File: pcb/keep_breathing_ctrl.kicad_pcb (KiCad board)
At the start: 4 copper layers, 112 x 131 mm, 177 parts, among them J2 Screw_Terminal, P1 CONN_RASPBERRY, Q1 PN2222, Q2 PN2222, U1 MPL3115A2, U10 PCF8523TK, U11 AQH3213AX, U12 AQH3213AX, U13 HTS221, U14 ICE40UP5K-SG48ITR, U15 GD25Q32CTIGR-Memory_Flash, U16 UCC12040, U17 ISO7762, U18 ZLDO1117G33TA, U2 powerSTEP01, U3 TLP240D, U4 TLP240D, U5 TLP240D, U6 TLP240D, U7 TLP240D, U8 TLP240D, U9 ZLDO1117G33TA, Y1 ABS06-107-32.768KHZ-T

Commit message: connecting SPI signals from STM32
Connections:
- U14 pad 10: (no net) -> /STM32F4/SPI3_MISO
- U14 pad 11: (no net) -> /STM32F4/SPI3_MOSI
- U14 pad 9: (no net) -> /STM32F4/SPI3_SCK
- U17 pad 5: (no net) -> /Power Stepper/M_CS
- UST1 pad 1: (no net) -> /Power Stepper/M_CLK
- UST1 pad 3: (no net) -> /Power Stepper/M_CS
- UST1 pad 4: (no net) -> /Power Stepper/M_MISO
- UST1 pad 5: (no net) -> /Power Stepper/M_MOSI
- UST1 pad 78: /Power Stepper/M_CLK -> /STM32F4/SPI3_SCK
- UST1 pad 79: /Power Stepper/M_MISO -> /STM32F4/SPI3_MISO
- UST1 pad 80: /Power Stepper/M_MOSI -> /STM32F4/SPI3_MOSI
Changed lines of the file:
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@@
     (zones 0)
     (modules 177)
-    (nets 137)
+    (nets 141)
   )
   (page A4)
@@
   (net 135 /SensorShields/SPI_CS_4)
   (net 136 /SensorShields/I2C_CLK_4)
+  (net 137 /STM32F4/SPI3_MOSI)
+  (net 138 /STM32F4/SPI3_MISO)
+  (net 139 /STM32F4/SPI3_SCK)
+  (net 140 "/Power Stepper/M_CS")
   (net_class Default "This is the default net class."
     (clearance 0.2)
@@
     (add_net /STM32F4/SDIO_D0)
     (add_net /STM32F4/SDIO_D1)
+    (add_net /STM32F4/SPI3_MISO)
+    (add_net /STM32F4/SPI3_MOSI)
+    (add_net /STM32F4/SPI3_SCK)
     (add_net /STM32F4/STM_I2C1_SCL)
     (add_net /STM32F4/STM_I2C1_SDA)
@@
     (add_net /SensorShields/SPI_MISO)
     (add_net /SensorShields/SPI_MOSI)
-    (add_net /SensorShields/SS_SPI_CLK)
     (add_net /SensorShields/SS_SPI_CS)
-    (add_net /SensorShields/SS_SPI_MISO)
-    (add_net /SensorShields/SS_SPI_MOSI)
     (add_net /SensorShields/VCC_PLL)
     (add_net /Sensors/SCL)
@@
     (add_net "Net-(U2-Pad63)")
     (add_net "Net-(U2-Pad64)")
-    (add_net "Net-(UST1-Pad1)")
     (add_net "Net-(UST1-Pad15)")
     (add_net "Net-(UST1-Pad16)")
     (add_net "Net-(UST1-Pad18)")
     (add_net "Net-(UST1-Pad2)")
-    (add_net "Net-(UST1-Pad3)")
     (add_net "Net-(UST1-Pad36)")
     (add_net "Net-(UST1-Pad38)")
-    (add_net "Net-(UST1-Pad4)")
     (add_net "Net-(UST1-Pad47)")
-    (add_net "Net-(UST1-Pad5)")
     (add_net "Net-(UST1-Pad55)")
     (add_net "Net-(UST1-Pad56)")
@@
     (pad 12 smd roundrect (at -3.4375 -2.75 315) (size 0.875 0.25) (layers B.Cu B.Paste B.Mask) (roundrect_rratio 0.25)
       (net 88 /SensorShields/I2C_CLK_2))
-    (pad 11 smd roundrect (at -3.4375 -2.25 315) (size 0.875 0.25) (layers B.Cu B.Paste B.Mask) (roundrect_rratio 0.25))
-    (pad 10 smd roundrect (at -3.4375 -1.75 315) (size 0.875 0.25) (layers B.Cu B.Paste B.Mask) (roundrect_rratio 0.25))
-    (pad 9 smd roundrect (at -3.4375 -1.25 315) (size 0.875 0.25) (layers B.Cu B.Paste B.Mask) (roundrect_rratio 0.25))
+    (pad 11 smd roundrect (at -3.4375 -2.25 315) (size 0.875 0.25) (layers B.Cu B.Paste B.Mask) (roundrect_rratio 0.25)
+      (net 137 /STM32F4/SPI3_MOSI))
+    (pad 10 smd roundrect (at -3.4375 -1.75 315) (size 0.875 0.25) (layers B.Cu B.Paste B.Mask) (roundrect_rratio 0.25)
+      (net 138 /STM32F4/SPI3_MISO))
+    (pad 9 smd roundrect (at -3.4375 -1.25 315) (size 0.875 0.25) (layers B.Cu B.Paste B.Mask) (roundrect_rratio 0.25)
+      (net 139 /STM32F4/SPI3_SCK))
     (pad 8 smd roundrect (at -3.4375 -0.75 315) (size 0.875 0.25) (layers B.Cu B.Paste B.Mask) (roundrect_rratio 0.25)
       (net 79 /SensorShields/CRESET_N))
@@
     (pad 81 smd roundrect (at 3.5 7.675 315) (size 0.3 1.6) (layers B.Cu B.Paste B.Mask) (roundrect_rratio 0.25))
     (pad 80 smd roundrect (at 4 7.675 315) (size 0.3 1.6) (layers B.Cu B.Paste B.Mask) (roundrect_rratio 0.25)
-      (net 57 "/Power Stepper/M_MOSI"))
+      (net 137 /STM32F4/SPI3_MOSI))
     (pad 79 smd roundrect (at 4.5 7.675 315) (size 0.3 1.6) (layers B.Cu B.Paste B.Mask) (roundrect_rratio 0.25)
-      (net 56 "/Power Stepper/M_MISO"))
+      (net 138 /STM32F4/SPI3_MISO))
     (pad 78 smd roundrect (at 5 7.675 315) (size 0.3 1.6) (layers B.Cu B.Paste B.Mask) (roundrect_rratio 0.25)
-      (net 58 "/Power Stepper/M_CLK"))
+      (net 139 /STM32F4/SPI3_SCK))
     (pad 77 smd roundrect (at 5.5 7.675 315) (size 0.3 1.6) (layers B.Cu B.Paste B.Mask) (roundrect_rratio 0.25)
       (net 130 /Rapsberry/JTDI))
@@
     (pad 6 smd roundrect (at -7.675 3.5 315) (size 1.6 0.3) (layers B.Cu B.Paste B.Mask) (roundrect_rratio 0.25)
       (net 59 +3.3VP))
-    (pad 5 smd roundrect (at -7.675 4 315) (size 1.6 0.3) (layers B.Cu B.Paste B.Mask) (roundrect_rratio 0.25))
-    (pad 4 smd roundrect (at -7.675 4.5 315) (size 1.6 0.3) (layers B.Cu B.Paste B.Mask) (roundrect_rratio 0.25))
-    (pad 3 smd roundrect (at -7.675 5 315) (size 1.6 0.3) (layers B.Cu B.Paste B.Mask) (roundrect_rratio 0.25))
+    (pad 5 smd roundrect (at -7.675 4 315) (size 1.6 0.3) (layers B.Cu B.Paste B.Mask) (roundrect_rratio 0.25)
+      (net 57 "/Power Stepper/M_MOSI"))
+    (pad 4 smd roundrect (at -7.675 4.5 315) (size 1.6 0.3) (layers B.Cu B.Paste B.Mask) (roundrect_rratio 0.25)
+      (net 56 "/Power Stepper/M_MISO"))
+    (pad 3 smd roundrect (at -7.675 5 315) (size 1.6 0.3) (layers B.Cu B.Paste B.Mask) (roundrect_rratio 0.25)
+      (net 140 "/Power Stepper/M_CS"))
     (pad 2 smd roundrect (at -7.675 5.5 315) (size 1.6 0.3) (layers B.Cu B.Paste B.Mask) (roundrect_rratio 0.25))
-    (pad 1 smd roundrect (at -7.675 6 315) (size 1.6 0.3) (layers B.Cu B.Paste B.Mask) (roundrect_rratio 0.25))
+    (pad 1 smd roundrect (at -7.675 6 315) (size 1.6 0.3) (layers B.Cu B.Paste B.Mask) (roundrect_rratio 0.25)
+      (net 58 "/Power Stepper/M_CLK"))
     (model ${KISYS3DMOD}/Package_QFP.3dshapes/LQFP-100_14x14mm_P0.5mm.wrl
       (at (xyz 0 0 0))
@@
     (pad 6 smd rect (at -2.6 -0.9525 90) (size 1.2 0.4) (layers B.Cu B.Paste B.Mask)
       (net 56 "/Power Stepper/M_MISO"))
-    (pad 5 smd rect (at -2.6 -0.3175 90) (size 1.2 0.4) (layers B.Cu B.Paste B.Mask))
+    (pad 5 smd rect (at -2.6 -0.3175 90) (size 1.2 0.4) (layers B.Cu B.Paste B.Mask)
+      (net 140 "/Power Stepper/M_CS"))
     (pad 4 smd rect (at -2.6 0.3175 90) (size 1.2 0.4) (layers B.Cu B.Paste B.Mask)
       (net 58 "/Power Stepper/M_CLK"))

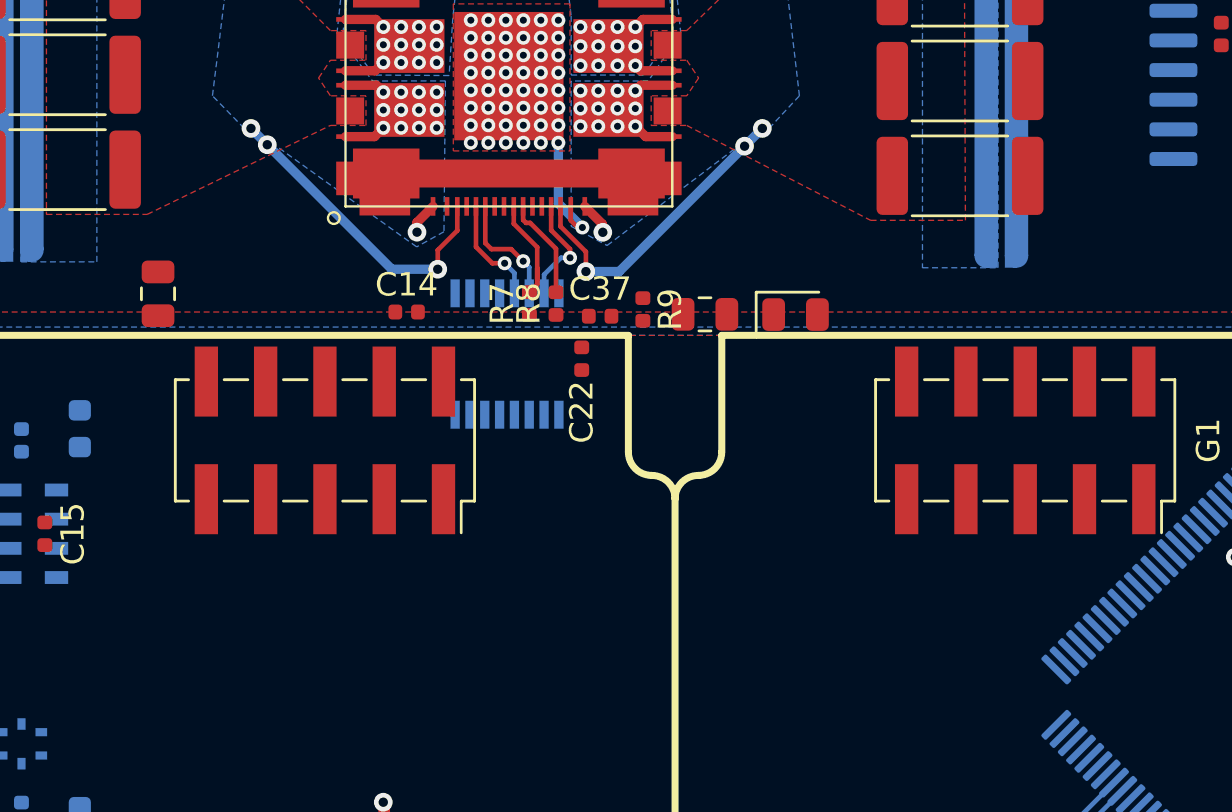
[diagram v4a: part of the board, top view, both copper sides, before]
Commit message: routing spi from stepper driver
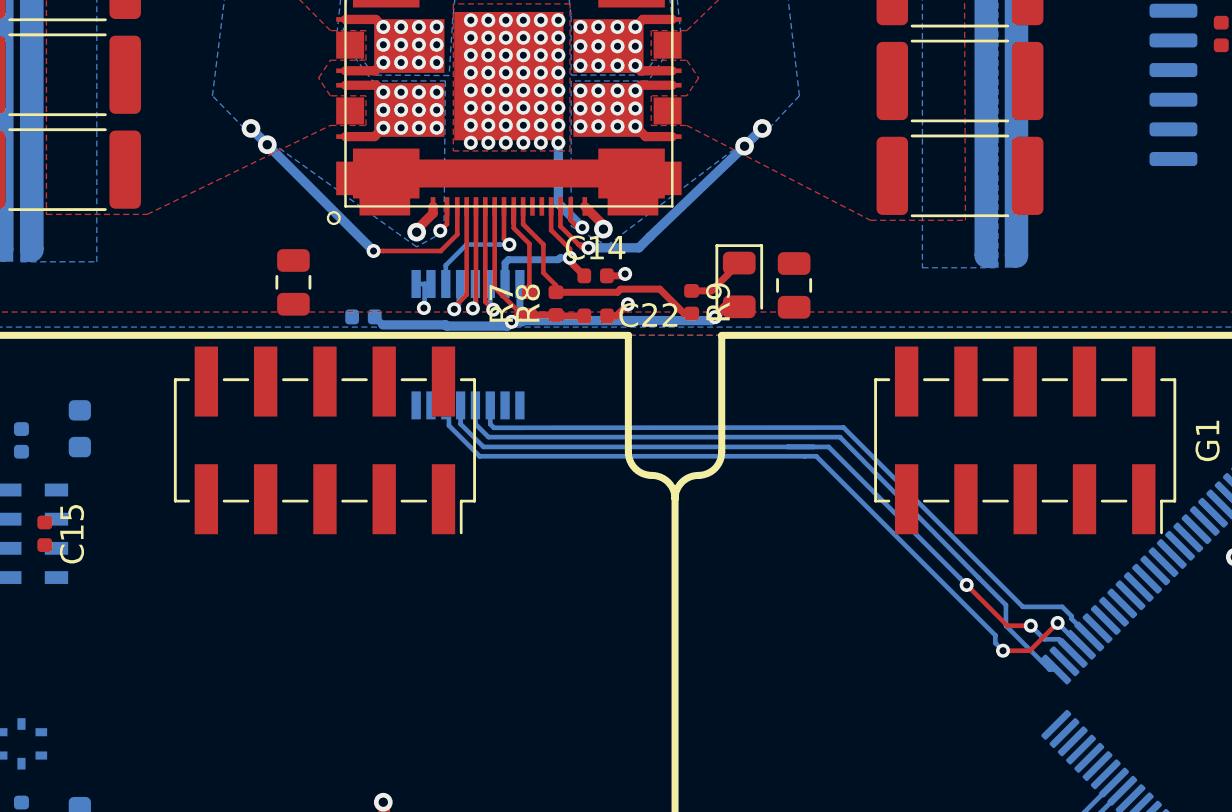
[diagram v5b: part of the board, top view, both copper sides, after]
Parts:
- C37: moved to B.Cu
- moved C37 10.1 mm to (97.2, 66.2), turned to 180 degrees
- moved C14 8.24 mm to (107.1, 64.5)
- moved C6 5.82 mm to (94.2, 64.7)
- moved C7 4.02 mm to (115.6, 64.9), turned to 270 degrees
- moved D5 2.72 mm to (113.2, 64.8), turned to 270 degrees
- moved R9 2.11 mm to (111.2, 65.6)
- moved C22 1.93 mm to (107.1, 66.2), turned to 0 degrees
- moved U17 1.72 mm to (101.6, 67.4)
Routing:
- net /Power Stepper/M_MISO: track 0.00 -> 33.1 mm, vias 0 -> 2
- net /Power Stepper/M_CS: track 0.00 -> 32.2 mm, vias 0 -> 2
- net /Power Stepper/M_CLK: track 0.00 -> 30.6 mm
- net /Power Stepper/M_MOSI: track 0.00 -> 30.3 mm
- net 3V3_M: track 18.4 -> 45.5 mm, vias 1 -> 3
- net SM_FLAG: track 4.36 -> 10.6 mm
- net /Power Stepper/SM_CS: track 0.00 -> 5.82 mm, vias 0 -> 1
- net /Power Stepper/SM_SO: track 0.00 -> 5.62 mm, vias 0 -> 1
- net GND_MOTOR: track 14.8 -> 19.6 mm, vias 54 -> 58
- net /Power Stepper/SM_RST: track 4.75 -> 7.34 mm
- net Net-(D5-Pad1): track 0.00 -> 2.53 mm
- net Net-(JP2-Pad1): track 13.5 -> 12.5 mm
- net Net-(JP1-Pad1): track 13.3 -> 12.4 mm
- net /Power Stepper/SM_CLK: track 4.72 -> 5.52 mm
- net /Power Stepper/SM_SI: track 5.00 -> 5.72 mm

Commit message: protection circuit added
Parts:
- removed C16, C76: 33u, Capacitor_SMD:C_1206_3216Metric
- removed C17: 220u, Capacitor_SMD:C_1206_3216Metric
- removed C18: 0.1u, Capacitor_SMD:C_0603_1608Metric
- removed C19: 1n, Capacitor_SMD:C_0603_1608Metric
- removed C77: 2.2uF, Capacitor_SMD:C_0603_1608Metric
- removed C79: 0.1u, Capacitor_SMD:C_0402_1005Metric
- removed D6: LED, LED_SMD:LED_0805_2012Metric
- removed U9: ZLDO1117G33TA, SMD:SOT-223
- added Q3: DMG2305UX, Package_TO_SOT_SMD:SOT-23, F.Cu at (1.42, 0.92)
- added Q4: BCM857BS, Package_TO_SOT_SMD:SOT-363_SC-70-6, F.Cu at (6.93, -2.72)
- added R2: 10k, Resistor_SMD:R_0402_1005Metric, F.Cu at (9.11, 2.19)
- C20: value 0.1u -> 100uF; footprint Capacitor_SMD:C_0603_1608Metric -> Resistor_SMD:R_1206_3216Metric
- C21: value 33u -> 47uF; footprint Capacitor_SMD:C_1206_3216Metric -> Resistor_SMD:R_0603_1608Metric
- C72: value 33u -> 100nF; footprint Capacitor_SMD:C_1206_3216Metric -> Resistor_SMD:R_0402_1005Metric
- C74: footprint Capacitor_SMD:C_0603_1608Metric -> Capacitor_SMD:C_0402_1005Metric
- C75: value 0.1u -> 1uF; footprint Capacitor_SMD:C_0402_1005Metric -> Capacitor_SMD:C_0603_1608Metric; moved to F.Cu
- R6: value 2k -> 47k
- U18: value ZLDO1117G33TA -> TCR8BM12; footprint SMD:SOT-223 -> SMD:DFN5B
- moved C20 271.8 mm to (2.00, -3.00), turned to 0 degrees
- moved C21 266.3 mm to (5.65, 0.46), turned to 0 degrees
- moved C74 251.1 mm to (14.5, -3.65)
- moved C72 242.5 mm to (9.11, 0.20)
- moved R6 242.0 mm to (12.0, -1.14), turned to 0 degrees
- moved U18 241.0 mm to (11.9, 1.38)
- moved C75 158.0 mm to (5.65, 2.97), turned to 0 degrees
- moved C73 157.0 mm to (11.1, -3.39), turned to 0 degrees
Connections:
- C20 pad 1: 3V3_STM -> +5V
- C21 pad 1: 3V3_STM -> +5V
- C74 pad 1: 3V3_ICE -> 1V2_ICE
- R6 pad 1: +5V -> Net-(Q3-Pad1)
- R6 pad 2: Net-(D6-Pad2) -> GND
- U18 pad 1: GND -> 1V2_ICE
- U18 pad 2: 3V3_ICE -> (no net)
- U18 pad 3: +5V -> (no net)
- U18 pad 4: 3V3_ICE -> +3V3

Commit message: mounting holes
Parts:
- added F1: MF-MSMF250/X, SMD:PTC, F.Cu at (64.0, 92.0)
- added H10: MountingHole, MountingHole:MountingHole_2.7mm_M2.5, F.Cu at (240.9, 35.0)
- added H5: MountingHole, MountingHole:MountingHole_2.7mm_M2.5, F.Cu at (75.0, 153.0)
- added H6: MountingHole, MountingHole:MountingHole_2.7mm_M2.5, F.Cu at (186.0, 30.5)
- added H7: MountingHole, MountingHole:MountingHole_2.7mm_M2.5, F.Cu at (75.0, 42.0)
- added H8: MountingHole, MountingHole:MountingHole_2.7mm_M2.5, F.Cu at (75.0, 104.0)
- added H9: MountingHole, MountingHole:MountingHole_2.7mm_M2.5, F.Cu at (186.0, 95.0)
- moved C20 99.0 mm to (63.0, 75.0)
- moved C21 99.0 mm to (66.7, 78.5)
- moved C72 99.0 mm to (70.1, 78.2)
- moved C73 99.0 mm to (72.1, 74.6)
- moved C74 99.0 mm to (75.5, 74.3)
- moved C75 99.0 mm to (66.7, 81.0)
- moved Q3 99.0 mm to (62.4, 78.9)
- moved Q4 99.0 mm to (67.9, 75.3)
- moved R2 99.0 mm to (70.1, 80.2)
- moved R6 99.0 mm to (73.0, 76.9)
- moved U18 99.0 mm to (72.9, 79.4)
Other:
- board size 112 x 131 mm -> 119.5 x 131 mm

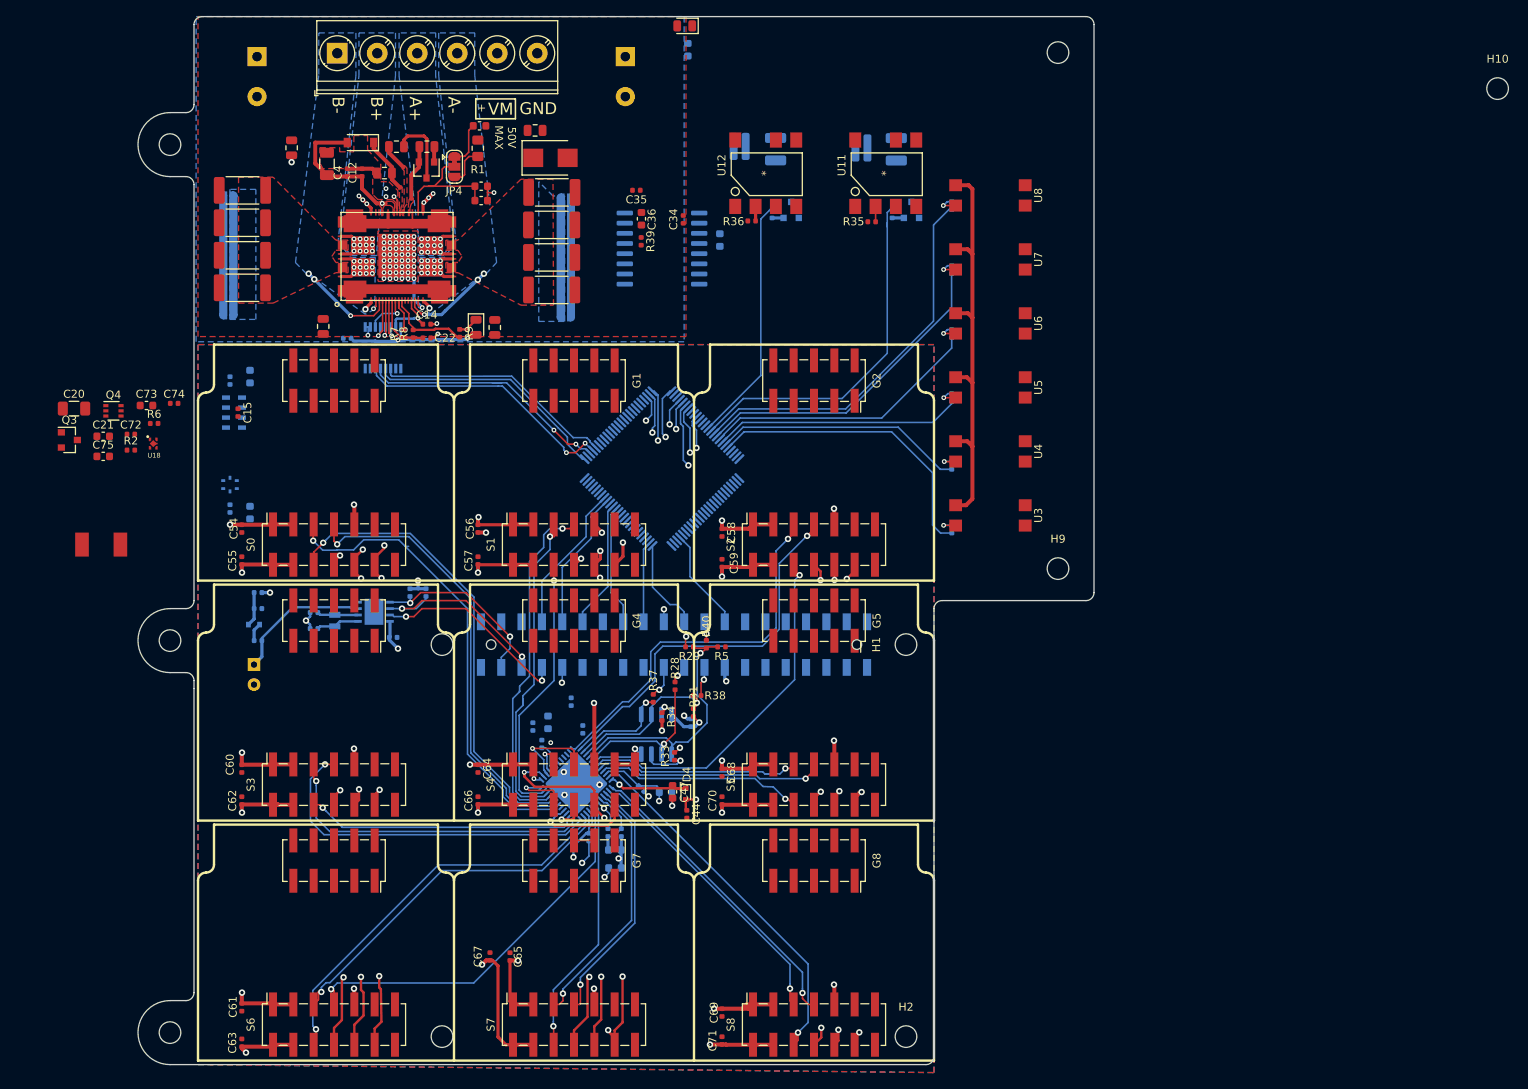
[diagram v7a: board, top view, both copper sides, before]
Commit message: adding  mounting holes
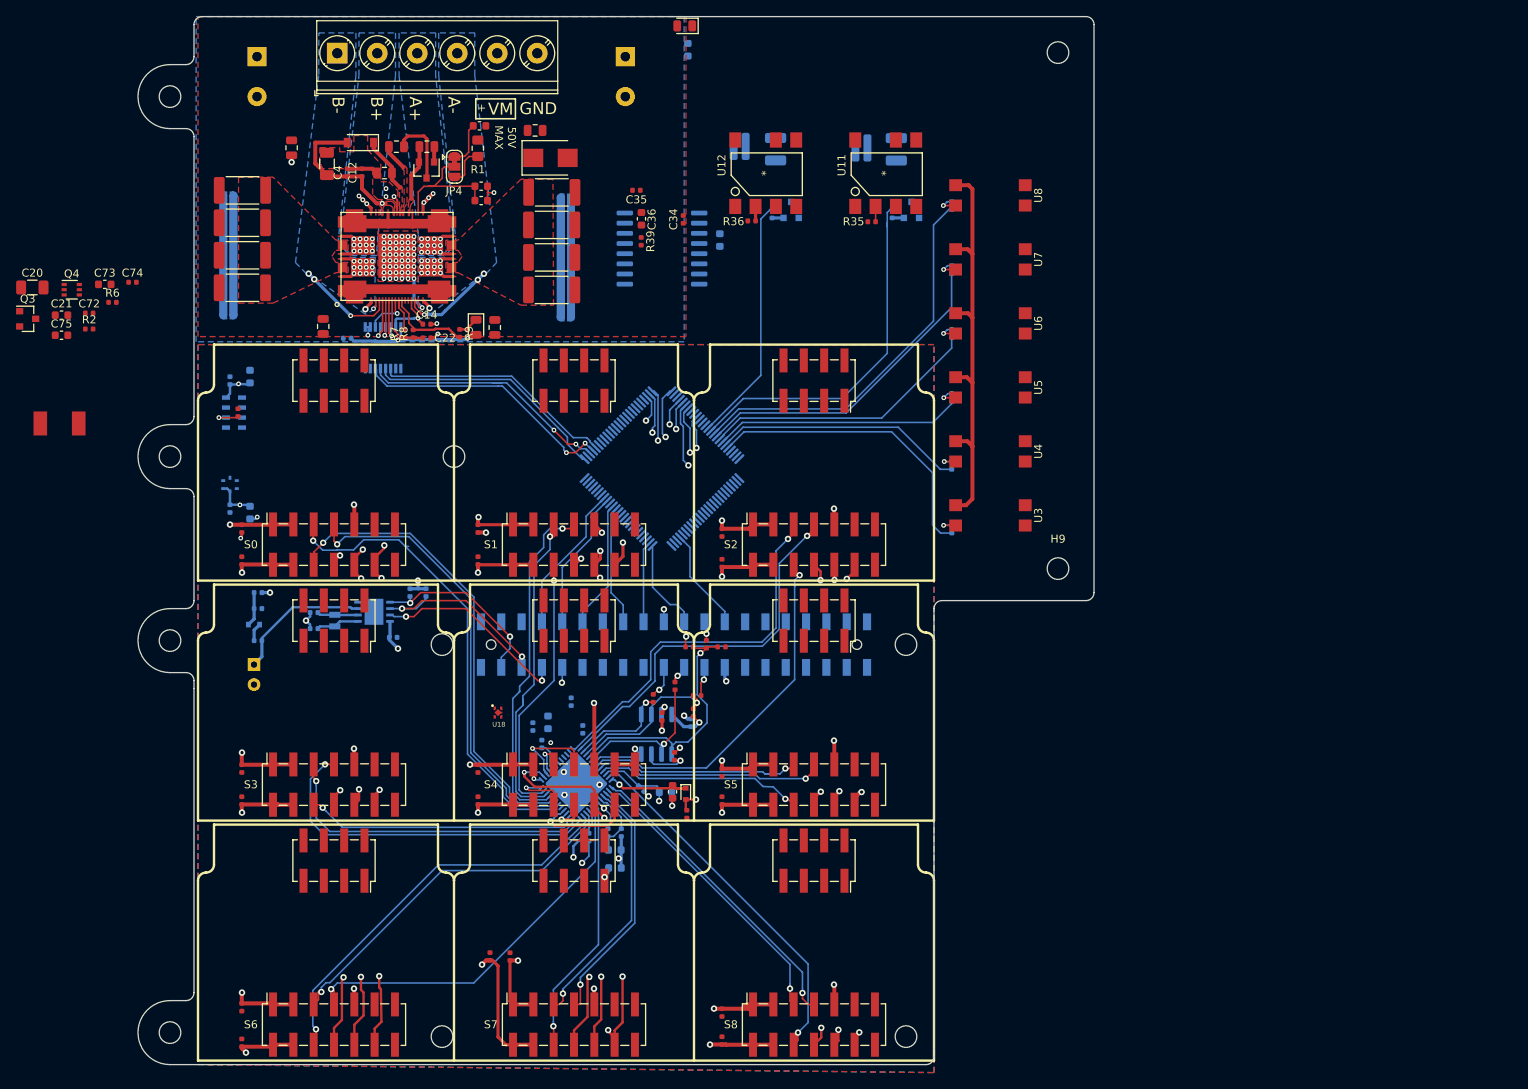
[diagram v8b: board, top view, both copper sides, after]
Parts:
- added H11: MountingHole, MountingHole:MountingHole_2.7mm_M2.5, F.Cu at (75.0, 81.0)
- G0, G1, G2, G3, G4, G5, G6, G7, G8: footprint Connector_PinSocket_2.54mm:PinSocket_2x05_P2.54mm_Vertical_SMD -> Connector_PinSocket_2.54mm:PinSocket_2x04_P2.54mm_Vertical_SMD
- moved H10 138.3 mm to (110.5, 81.0)
- moved U18 54.7 mm to (116.0, 113.0)
- moved C73 16.0 mm to (66.8, 59.5)
- moved C75 16.0 mm to (61.4, 65.8)
- moved Q4 16.0 mm to (62.7, 60.1)
- moved C20 16.0 mm to (57.8, 59.9)
- moved F1 16.0 mm to (58.8, 76.9)
- moved Q3 16.0 mm to (57.2, 63.8)
- moved C21 16.0 mm to (61.4, 63.3)
- moved C72 16.0 mm to (64.9, 63.1)
- moved R2 16.0 mm to (64.9, 65.0)
- moved R6 16.0 mm to (67.8, 61.7)
- moved C74 16.0 mm to (70.3, 59.2)
- moved H7 6.00 mm to (75.0, 36.0)
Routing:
- net +3V3: track 110.7 -> 120.5 mm, vias 20 -> 22
- net Net-(C15-Pad1): track 0.00 -> 3.34 mm, vias 0 -> 1
- net GND: track 31.7 -> 33.5 mm, vias 14 -> 16
- removed copper zone on B.Cu, net Net-(JP1-Pad1)
- removed copper zone on B.Cu, net Net-(JP2-Pad1)
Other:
- outline, holes or cut-outs redrawn
